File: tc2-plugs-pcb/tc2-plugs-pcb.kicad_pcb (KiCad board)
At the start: 4 copper layers, 57.5 x 28 mm, 51 parts, among them J101 JCON_M12_02Pin, J102 JCON_M16_04Pin, J103 Conn_02x04_Odd_Even, Q101 Q_PMOS_GSD, U101 TPS54331, U102 TPS54331

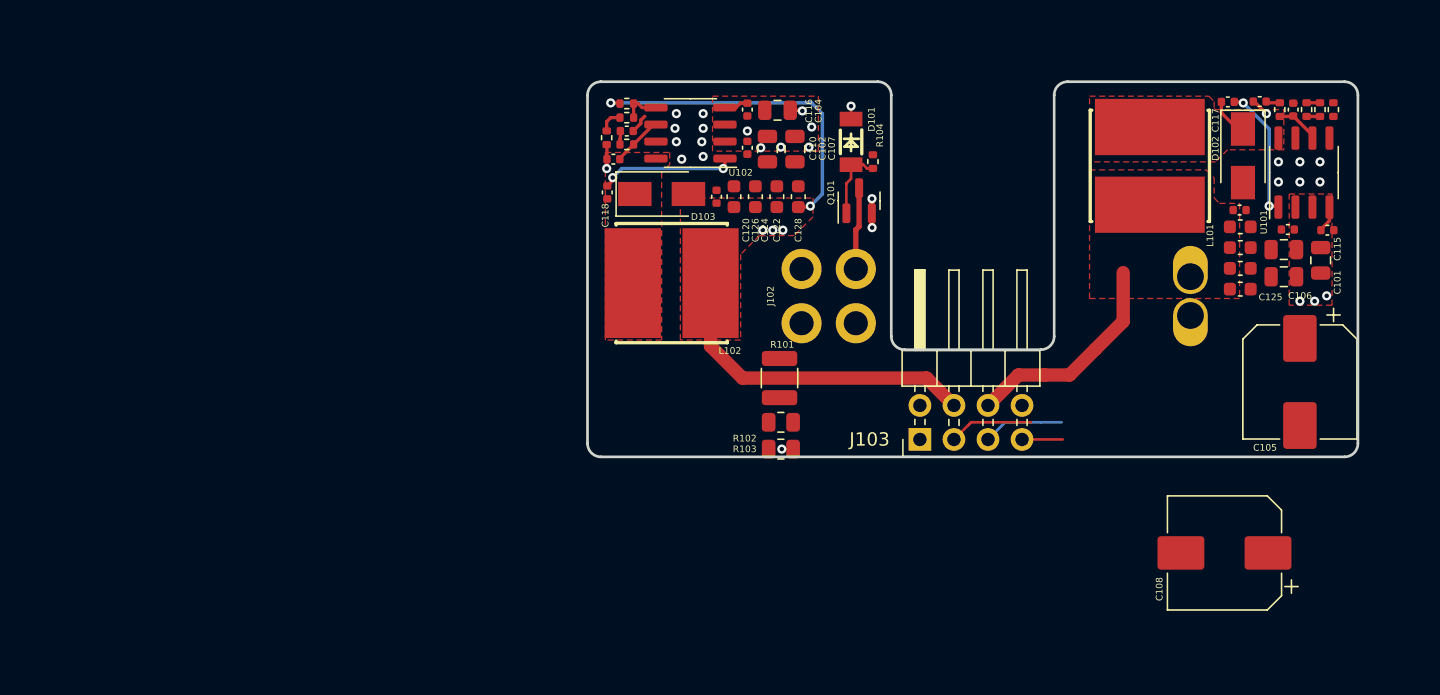
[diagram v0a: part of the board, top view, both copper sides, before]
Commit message: Clean up of files and updated drawings for PCBs
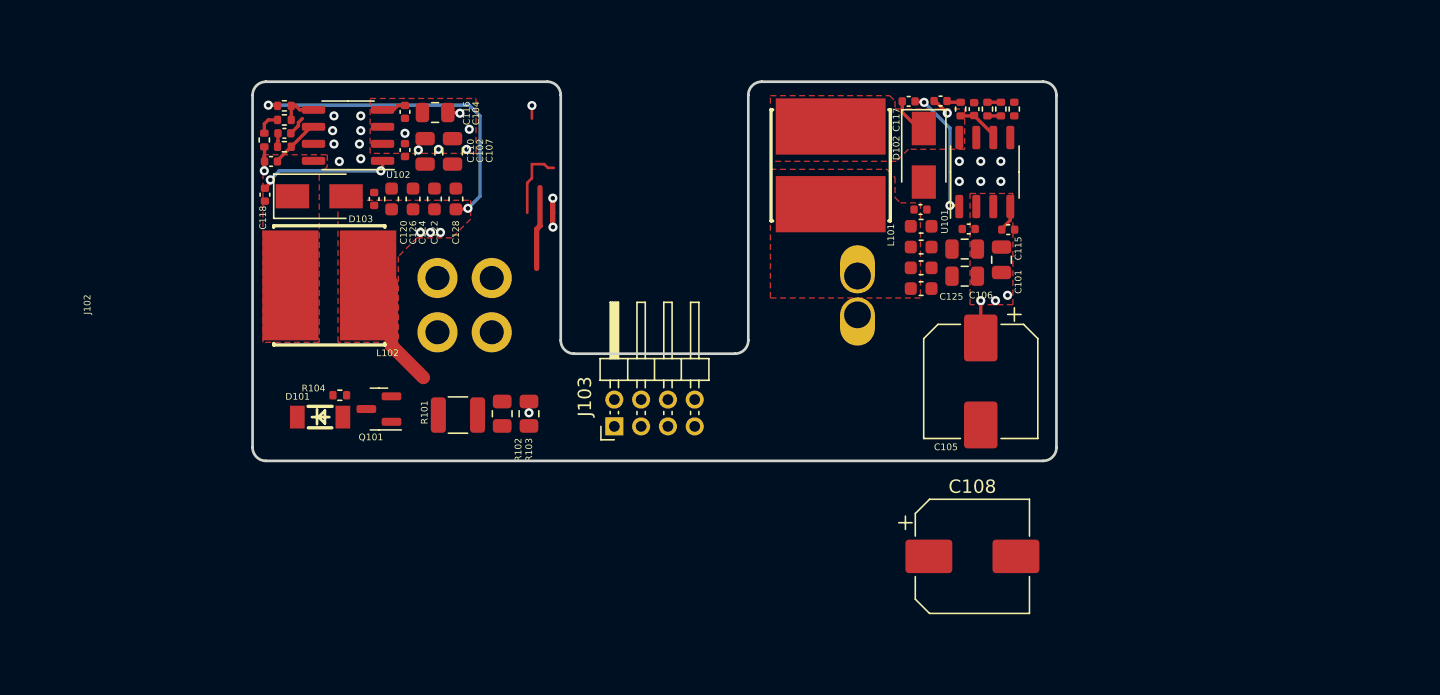
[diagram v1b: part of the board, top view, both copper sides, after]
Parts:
- J103: footprint Connector_PinHeader_2.54mm:PinHeader_2x04_P2.54mm_Horizontal -> Connector_PinHeader_2.00mm:PinHeader_2x04_P2.00mm_Horizontal
- moved D101 44.6 mm to (75.0, 125.0), turned to 0 degrees
- moved R104 43.4 mm to (76.5, 123.4), turned to 180 degrees
- moved Q101 39.1 mm to (79.4, 124.4), turned to 180 degrees
- moved J102 27.2 mm to (85.8, 116.7)
- moved C102 25.6 mm to (82.9, 105.2)
- moved C104 25.6 mm to (83.6, 102.3)
- moved C107 25.6 mm to (84.9, 105.2)
- moved C110 25.6 mm to (81.4, 105.1)
- moved C112 25.6 mm to (72.4, 103.8)
- moved C114 25.6 mm to (71.4, 106.0)
- moved C116 25.6 mm to (81.4, 102.2)
- moved C124 25.6 mm to (82.0, 108.8)
- moved C126 25.6 mm to (80.4, 108.8)
- moved C128 25.6 mm to (85.2, 108.8)
- moved D103 25.6 mm to (75.0, 108.5)
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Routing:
- net +3V3: track 49.8 -> 33.1 mm
- net +5V: track 16.3 -> 0.00 mm
- net 5V_EN: track 6.28 -> 0.00 mm
- net /Speaker-: track 6.02 -> 0.00 mm
- net /Speaker+: track 3.04 -> 0.00 mm
- net +12V: track 3.14 -> 5.92 mm
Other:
- board size 57.5 x 28 mm -> 60 x 28.3 mm

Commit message: Version 2 WIP
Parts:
- removed C108: 220uF, Capacitor_SMD:CP_Elec_8x10
- D101: footprint cacophony-footprints:LL-34_L3.5-W1.5-RD -> cacophony-library:LL-34_L3.5-W1.5-RD
- J103: footprint Connector_PinHeader_2.00mm:PinHeader_2x04_P2.00mm_Horizontal -> cacophony-library:PinHeader_2x04_P2.00mm_Horizontal
- L101, L102: footprint cacophony-footprints:IND-SMD_L8.0-W8.0_1217AS -> cacophony-library:IND-SMD_L8.0-W8.0_1217AS
- moved D101 25.6 mm to (89.7, 104.0), turned to -90 degrees
- moved R104 23.3 mm to (91.4, 105.5), turned to 90 degrees
- moved Q101 19.4 mm to (90.3, 108.4), turned to -90 degrees
- moved R102 4.85 mm to (84.0, 126.2), turned to 0 degrees
- moved R103 3.56 mm to (87.4, 126.2), turned to 0 degrees
- moved J103 3.32 mm to (100.0, 124.3)
- moved J101 2.97 mm to (118.0, 116.8)
- moved R101 2.42 mm to (84.0, 122.9), turned to -90 degrees
- moved R110 1.83 mm to (128.7, 102.0)
- moved C109 1.83 mm to (125.3, 111.0)
- moved C111 1.83 mm to (123.2, 101.4)
- moved C113 1.83 mm to (125.7, 102.0)
- moved C117 1.83 mm to (120.8, 101.5)
- moved C119 1.83 mm to (121.7, 109.5)
- moved D102 1.83 mm to (121.9, 105.5)
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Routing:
- net 5V_EN: track 0.00 -> 41.1 mm, vias 0 -> 1
- net +5V: track 0.00 -> 38.4 mm, vias 0 -> 2
- net /Speaker-: track 0.00 -> 21.1 mm
- net +3V3: track 33.1 -> 53.3 mm, vias 5 -> 2
- net /Speaker+: track 0.00 -> 18.7 mm
- net /Batt_sense: track 0.00 -> 15.9 mm
- net VIN: track 6.13 -> 0.00 mm
- net +12V: track 5.92 -> 1.29 mm, vias 11 -> 13
- net Net-(U101-VSENSE): track 1.00 -> 4.32 mm
- net /+Batt: track 0.00 -> 2.58 mm
- net Net-(D101-A): track 5.52 -> 3.25 mm
- net Net-(R102-Pad2): track 0.00 -> 1.55 mm
- net GND: track 6.80 -> 7.65 mm
- added copper zone on F.Cu, net VIN

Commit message: P2 milestone
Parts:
- removed J101: JCON_M12_02Pin, cacophony-library:jcon-2pin-m12
- added C108: 10uF, Capacitor_SMD:C_0603_1608Metric, F.Cu at (23.1, 1.28)
- added C129: 10uF, Capacitor_SMD:C_0603_1608Metric, F.Cu at (20.8, 2.34)
- added J104: Conn_02x06_Odd_Even, cacophony-library:PinHeader_2x06_P2.00mm_Horizontal, F.Cu at (-5.00, 1.00)
- added Q102: Q_PMOS_GSD, Package_TO_SOT_SMD:SOT-23, F.Cu at (20.4, -0.09)
- added Q103: 2N7002, Package_TO_SOT_SMD:SOT-23, F.Cu at (15.4, 1.71)
- added R113: 100k, Resistor_SMD:R_0402_1005Metric, F.Cu at (18.0, -0.10)
- added R114: 1k, Resistor_SMD:R_0402_1005Metric, F.Cu at (12.9, 1.92)
- added TP101: TestPoint_2Pole, cacophony-library:test-point-2p, F.Cu at (24.7, 1.37)
- J103: value Conn_02x04_Odd_Even -> JCON_M16_06Pin; footprint cacophony-library:PinHeader_2x04_P2.00mm_Horizontal -> cacophony-library:jcon-6pin-m16
- moved J102 159.8 mm to (-15.0, -6.97)
- moved R101 159.6 mm to (-16.4, -1.16)
- moved R102 159.6 mm to (-16.4, 2.14)
- moved R103 159.6 mm to (-13.1, 2.15)
- moved D101 158.2 mm to (-11.5, -17.6), turned to 90 degrees
- moved Q101 158.2 mm to (-10.9, -13.2)
- moved R104 158.2 mm to (-9.87, -16.1)
- moved C122 157.4 mm to (-16.8, -12.9)
- moved C124 157.4 mm to (-18.2, -12.9)
- moved C126 157.4 mm to (-19.7, -12.9)
- moved C128 157.4 mm to (-15.3, -12.9)
- moved C118 157.2 mm to (-29.0, -12.9)
- moved L102 157.2 mm to (-24.2, -6.15)
- moved C110 157.2 mm to (-18.6, -16.2)
- moved C120 157.2 mm to (-20.9, -12.6)
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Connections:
- J103 pad 1: /Batt_sense -> GND
- J103 pad 2: GND -> OUT_RX
- J103 pad 3: 5V_EN -> OUT_TX
- J103 pad 4: +3V3 -> SPEAKER_+
- J103 pad 5: /Speaker- -> SPEAKER_-
- J103 pad 6: +5V -> VOUT
- R101 pad 2: /Batt_sense -> BATT_SENSE
- R102 pad 1: /Batt_sense -> BATT_SENSE
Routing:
- net SPEAKER_+: track 0.00 -> 33.0 mm
- net SPEAKER_-: track 0.00 -> 30.4 mm
- net OUT_TX: track 0.00 -> 21.9 mm
- net /Speaker-: track 21.1 -> 0.00 mm
- net /Speaker+: track 18.7 -> 0.00 mm
- net OUT_RX: track 0.00 -> 17.4 mm
- net EN_PERIPH: track 0.00 -> 16.4 mm, vias 0 -> 2
- net /Batt_sense: track 15.9 -> 0.00 mm
- net BATT_SENSE: track 0.00 -> 13.9 mm
- net +5V: track 38.4 -> 47.2 mm
- net Net-(Q102-G): track 0.00 -> 5.21 mm
- net 5V_EN: track 41.1 -> 45.2 mm
- net Net-(D101-A): track 3.25 -> 7.25 mm
- net +3V3: track 53.3 -> 51.4 mm
- net Net-(Q103-G): track 0.00 -> 1.92 mm
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- added copper zone on F.Cu, net VOUT
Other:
- board size 60 x 28.3 mm -> 65 x 28.3 mm

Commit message: P3-Nov release
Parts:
- removed J103: JCON_M16_06Pin, cacophony-library:jcon-6pin-m16
- removed Q103: 2N7002, Package_TO_SOT_SMD:SOT-23
- added FB1: FerriteBead, Inductor_SMD:L_0805_2012Metric, F.Cu at (-15.3, -1.89)
- added FB2: FerriteBead, Inductor_SMD:L_0805_2012Metric, F.Cu at (11.8, -5.51)
- added J101: JCON_M16_2+4Pin, cacophony-library:jcon-2+4pin-m16, F.Cu at (22.0, -7.00)
- added Q1: AO3400A, Package_TO_SOT_SMD:SOT-23, F.Cu at (15.4, 1.71)
- added R1: 100k, Resistor_SMD:R_0402_1005Metric, F.Cu at (13.1, 2.48)
- added R115: 2M, Resistor_SMD:R_1210_3225Metric, F.Cu at (-20.1, 1.58)
- added R116: 560k, Resistor_SMD:R_1206_3216Metric, F.Cu at (-16.2, 2.70)
- added R117: 33k, Resistor_SMD:R_0603_1608Metric, F.Cu at (-12.5, 2.70)
- added TP102: TestPoint_2Pole, cacophony-library:test-point-2p, F.Cu at (9.78, -7.01)
- added TP103: TestPoint_2Pole, cacophony-library:test-point-2p, F.Cu at (-9.84, -0.55)
- moved R110 62.2 mm to (-28.3, -19.0), turned to 180 degrees
- moved R112 61.5 mm to (34.1, -21.3), turned to -90 degrees
- moved R107 61.3 mm to (-28.3, -18.0), turned to 0 degrees
- moved R109 60.8 mm to (31.6, -22.8), turned to 180 degrees
- moved R108 60.6 mm to (33.1, -21.3), turned to -90 degrees
- moved R111 60.5 mm to (-28.3, -17.1), turned to 0 degrees
- moved C113 59.7 mm to (-28.3, -16.1), turned to 180 degrees
- moved C112 59.6 mm to (32.1, -21.3), turned to -90 degrees
- moved R105 58.8 mm to (-28.3, -15.2), turned to 180 degrees
- moved R106 58.7 mm to (31.1, -21.3), turned to 90 degrees
- moved C111 58.4 mm to (-28.9, -13.8), turned to -90 degrees
- moved C114 58.3 mm to (30.0, -21.8), turned to 90 degrees
- moved C118 57.5 mm to (27.7, -22.9), turned to 180 degrees
- moved C117 56.4 mm to (-28.9, -11.4), turned to -90 degrees
- moved U101 55.3 mm to (-23.6, -16.9), turned to 180 degrees
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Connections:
- C119 pad 1: +5V -> /5V0_PF
- C120 pad 1: +3V3 -> /3V3_PF
- C121 pad 1: +5V -> /5V0_PF
- C122 pad 1: +3V3 -> /3V3_PF
- C123 pad 1: +5V -> /5V0_PF
- C124 pad 1: +3V3 -> /3V3_PF
- C125 pad 1: +5V -> /5V0_PF
- C126 pad 1: +3V3 -> /3V3_PF
- C127 pad 1: +5V -> /5V0_PF
- C128 pad 1: +3V3 -> /3V3_PF
- J104 pad 1: BATT_SENSE -> 5V_EN
- J104 pad 10: unconnected-(J104-Pin_10-Pad10) -> +3V3
- J104 pad 11: OUT_RX -> EN_PERIPH_POWER
- J104 pad 12: EN_PERIPH -> GND
- J104 pad 2: GND -> OUT_RX
- J104 pad 3: 5V_EN -> BATT_SENSE_HV
- J104 pad 4: +3V3 -> OUT_TX
- J104 pad 5: SPEAKER_+ -> BATT_SENSE_LV
- J104 pad 6: +5V -> GND
- J104 pad 8: GND -> +5V
- J104 pad 9: OUT_TX -> SPEAKER_+
- L101 pad 2: +5V -> /5V0_PF
- L102 pad 2: +3V3 -> /3V3_PF
- R101 pad 2: BATT_SENSE -> BATT_SENSE_HV
- R102 pad 1: BATT_SENSE -> BATT_SENSE_HV
- R110 pad 1: +5V -> /5V0_PF
- R112 pad 1: +3V3 -> /3V3_PF
- R114 pad 1: EN_PERIPH -> EN_PERIPH_POWER
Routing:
- net +3V3: track 51.4 -> 11.3 mm, vias 2 -> 0
- net /3V3_PF: track 0.00 -> 33.1 mm, vias 0 -> 2
- net +5V: track 47.2 -> 17.4 mm, vias 2 -> 0
- net BATT_SENSE_HV: track 0.00 -> 25.9 mm
- net /5V0_PF: track 0.00 -> 22.5 mm, vias 0 -> 2
- net BATT_SENSE_LV: track 0.00 -> 20.8 mm
- net 5V_EN: track 45.2 -> 28.8 mm
- net EN_PERIPH: track 16.4 -> 0.00 mm, vias 2 -> 0
- net BATT_SENSE: track 13.9 -> 0.00 mm
- net /+Batt: track 2.58 -> 14.0 mm, vias 0 -> 1
- net OUT_RX: track 17.4 -> 27.6 mm, vias 0 -> 1
- net EN_PERIPH_POWER: track 0.00 -> 7.44 mm, vias 0 -> 2
- net OUT_TX: track 21.9 -> 28.3 mm
- net SPEAKER_-: track 30.4 -> 33.5 mm, vias 0 -> 4
- net SPEAKER_+: track 33.0 -> 30.3 mm
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- added copper zone on F.Cu, net /3V3_PF
- added copper zone on F.Cu, net /5V0_PF
- removed copper zone on F.Cu, net +3V3
- removed copper zone on F.Cu, net +5V
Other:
- board text added: "+Batt"
- board text added: "3V3"
- board text added: "5V"
- board text added: "GND"
- board text added: "RX"
- board text added: "TX"
- board text added: "V0.1.3"
- board text added: "VIN"
- board text added: "VOUT"
